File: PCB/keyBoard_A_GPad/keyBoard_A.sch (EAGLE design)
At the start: 289 parts, among them IC1 74HC04N, IC2 LMV358IDGKR, J1 J, J10 J, J11 J, J12 J, J13 J, J14 J, J15 J, J16 J, J17 J, J18 J, J19 J, J2 J, J20 J, J21 J, J22 J, J23 J, J24 J, J25 J, J26 J, J27 J, J28 J, J29 J, J3 J, J30 J, J31 J, J32 J, J33 J, J34 J, J35 J, J36 J, J37 J, J38 J, J39 J, J4 J, J40 J, J41 J, J42 J, J43 J, J44 J, J45 J, J47 USB MICRO, J5 J, J6 J, J7 J, J8 J, J9 J, Y1 16MHz KX-7, Y2 16MHz KX-7

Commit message: add kesize table. bad pcb a b
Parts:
- added 2D1: 74HC138N, detali2:74AC138N
- added 2D2: 74HC04N, detali2:74ALS04N
- added C19: 100n, rcl:C-EUC0805
- added C20: 100n, rcl:C-EUC1206
- added D49, D50, D51, D52, D53, D54, D55, D56, D57, D58, D59, D60, D61, D62, D63, D64, D64B, D65, D66, D67, D67B, D68, D69, D70, D71, D72, D73, D74, D75, D76, D77, D78, D79, D80, D81, D82, D83, D84, D85, D86, D87, D88, D89, D92, D93: LL4148, detali:LL4148
- added J46, J48, J49, J50, J51, J52, J53, J54, J55, J56, J57, J58, J59, J60, J61, J62, J63, J64, J65, J66, J67, J68, J69, J70, J71, J72, J73, J74, J75, J76, J77, J78, J79, J80, J81, J82, J83, J84, J85, J86, J87, J88, J89, J90, J91, J92, J93, J94, J95, J96: J, detali2:J
- added JA47, JA48, JA49, JA50, JA51, JA52, JA53, JA54, JA55, JA56, JA57, JA58, JA59, JA60, JA61, JA62, JA63, JA64, JA65, JA66, JA67, JA67B, JA67B1, JA68, JA69, JA70, JA71, JA72, JA73, JA74, JA74B, JA75, JA76, JA77, JA78, JA79, JA80, JA81, JA82, JA83, JA84, JA85, JA86, JA87, JB47, JB48, JB49, JB50, JB51, JB52, JB53, JB54, JB55, JB56, JB57, JB58, JB59, JB60, JB61, JB62, JB63, JB64, JB65, JB66, JB67, JB67B, JB68, JB69, JB70, JB71, JB72, JB73, JB74, JB74B, JB75, JB76, JB77, JB78, JB79, JB80, JB81, JB82, JB83, JB84, JB85, JB86, JB87: (no value), detali:SJ
- added R16: 1k, rcl:R-EU_R0805
- added R17, R18, R19, R21, R22: 10k, rcl:R-EU_R0805
- added R20: 10k, rcl:R-EU_R1206W
- added S47: F7, cherrymx:CHERRY-MX-4P
- added S48: F8, cherrymx:CHERRY-MX-4P
- added S49: F9, cherrymx:CHERRY-MX-4P
- added S50: F10, cherrymx:CHERRY-MX-4P
- added S51: F11, cherrymx:CHERRY-MX-4P
- added S52: F12, cherrymx:CHERRY-MX-4P
- added S53: 7, cherrymx:CHERRY-MX-4P
- added S54: 8, cherrymx:CHERRY-MX-4P
- added S55: 9, cherrymx:CHERRY-MX-4P
- added S56: 0, cherrymx:CHERRY-MX-4P
- added S57: -, cherrymx:CHERRY-MX-4P
- added S58: =, cherrymx:CHERRY-MX-4P
- added S59: BS, cherrymx:CHERRY-MX-4P
- added S60: Y, cherrymx:CHERRY-MX-4P
- added S61: U, cherrymx:CHERRY-MX-4P
- added S62: I, cherrymx:CHERRY-MX-4P
- added S63: O, cherrymx:CHERRY-MX-4P
- added S64: P, cherrymx:CHERRY-MX-4P
- added S65: [, cherrymx:CHERRY-MX-4P
- added S66: ], cherrymx:CHERRY-MX-4P
- added S67: |d, cherrymx:CHERRY-MX-4P
- added S67B: |u, cherrymx:CHERRY-MX
- added S67C: |, cherrymx:CHERRY-MX-4P
- added S68: H, cherrymx:CHERRY-MX-4P
- added S69: J, cherrymx:CHERRY-MX-4P
- added S70: K, cherrymx:CHERRY-MX-4P
- added S71: L, cherrymx:CHERRY-MX-4P
- added S72: :, cherrymx:CHERRY-MX-4P
- added S73: ", cherrymx:CHERRY-MX-4P
- added S74: Del, cherrymx:CHERRY-MX-4P
- added S74A: Enter, cherrymx:CHERRY-MX-4P
- added S74B: Enter, cherrymx:CHERRY-MX
- added S75: N, cherrymx:CHERRY-MX-4P
- added S76: M, cherrymx:CHERRY-MX-4P
- added S77: <, cherrymx:CHERRY-MX-4P
- added S78: >, cherrymx:CHERRY-MX-4P
- added S79: ~, cherrymx:CHERRY-MX-4P
- added S80: ?, cherrymx:CHERRY-MX-4P
- added S81: R Shift, cherrymx:CHERRY-MX-4P
- added S82: Space, cherrymx:CHERRY-MX-4P
- added S83: FN3, cherrymx:CHERRY-MX-4P
- added S84: R_Alt, cherrymx:CHERRY-MX-4P
- added S85: RCtrl, cherrymx:CHERRY-MX-4P
- added S86: PrtScr, cherrymx:CHERRY-MX-4P
- added S87: FN2, cherrymx:CHERRY-MX-4P
- added SV4: CON_KB_B, detali2:FE12-1
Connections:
- new net +3VD: 2D2P.VCC, C20.1, D92.C
- new net 2I: 2D1A.Y1, D50.C, J95.P$1
- new net 8J: D79.C, D84.C, D85.C, D89.C, J87.P$1
- new net G1: 2D2D.I, JA47.2, JA48.2, JA49.2, JA53.2, JA60.2, JA68.2, JA75.2, JA82.2, R17.2
- new net G2: J63.P$2, JA54.2, JA55.2, JA56.2, JA61.2, JA69.2, JA70.2, JA76.2, JA77.2, R18.2
- new net G3: J57.P$2, JA62.2, JA63.2, JA71.2
- new net G4: J76.P$2, JA50.2, JA51.2, JA57.2, JA64.2, JA72.2, JA78.2, JA79.2, JA87.2
- new net G5: J62.P$2, JA52.2, JA58.2, JA65.2, JA66.2, JA73.2, JA80.2, JA83.2, JA84.2
- new net G6: J59.P$2, JA59.2, JA67.2, JA67B.2, JA67B1.2, JA74B.2, JA81.2, JA85.2, JA86.2, JB74.1
- new net GG5: 2D2E.I, J61.P$1, R21.2
- new net N$107: JB52.2, S52G$1.PIN-1
- new net N$151: JB63.2, S63G$1.PIN-1
- new net N$229: JB74.2, S74AG$1.PIN-1, S74B.PIN-1
- new net N$230: JA74.1, S74AG$1.PIN-2, S74B.PIN-2
- new net N$233: JB47.2, S47G$1.PIN-1
- new net N$234: JB53.2, S53G$1.PIN-1
- new net N$235: JB60.2, S60G$1.PIN-1
- new net N$236: JB68.2, S68G$1.PIN-1
- new net N$237: JB75.2, S75G$1.PIN-1
- new net N$238: JB82.2, S82G$1.PIN-1
- new net N$239: JB48.2, S48G$1.PIN-1
- new net N$240: JB54.2, S54G$1.PIN-1
- new net N$241: JB61.2, S61G$1.PIN-1
- new net N$242: JB69.2, S69G$1.PIN-1
- new net N$243: JB49.2, S49G$1.PIN-1
- new net N$244: JB55.2, S55G$1.PIN-1
- new net N$245: JB70.2, S70G$1.PIN-1
- new net N$246: JB77.2, S77G$1.PIN-1
- new net N$247: JB56.2, S56G$1.PIN-1
- new net N$248: JB51.2, S51G$1.PIN-1
- new net N$249: D49.A, JB47.1
- new net N$250: D55.A, JB53.1
- new net N$251: D62.A, JB60.1
- new net N$252: D70.A, JB68.1
- new net N$253: D77.A, JB75.1
- new net N$254: D84.A, JB82.1
- new net N$255: D50.A, JB48.1
- new net N$256: D56.A, JB54.1
- new net N$257: D63.A, JB61.1
- new net N$258: D71.A, JB69.1
- new net N$259: D78.A, JB76.1
- new net N$260: D85.A, JB83.1
- new net N$261: D51.A, JB49.1
- new net N$262: D57.A, JB55.1
- new net N$263: D64.A, JB62.1
- new net N$264: D72.A, JB70.1
- new net N$265: D79.A, JB77.1
- new net N$266: D86.A, JB84.1
- new net N$267: D52.A, JB50.1
- new net N$268: D58.A, JB56.1
- new net N$269: D65.A, JB63.1
- new net N$270: D73.A, JB71.1
- new net N$271: D80.A, JB78.1
- new net N$272: D87.A, JB85.1
- new net N$274: D53.A, JB51.1
- new net N$275: D59.A, JB57.1
- new net N$277: D66.A, JB64.1
- new net N$278: D74.A, JB72.1
- new net N$279: D81.A, JB79.1
- new net N$280: D88.A, JB86.1
- new net N$281: D54.A, JB52.1
- new net N$282: D60.A, JB58.1
- new net N$283: D67.A, JB65.1
- new net N$285: D75.A, JB73.1
- new net N$286: D82.A, JB80.1
- new net N$287: D61.A, JB59.1
- new net N$288: D68.A, JB66.1
- new net N$289: D69.A, JB67.1
- new net N$290: D83.A, JB81.1
- new net N$291: JA47.1, S47G$1.PIN-2
- new net N$292: JA53.1, S53G$1.PIN-2
- new net N$293: JA60.1, S60G$1.PIN-2
- new net N$294: JA68.1, S68G$1.PIN-2
- new net N$295: JA75.1, S75G$1.PIN-2
- new net N$296: JA82.1, S82G$1.PIN-2
- new net N$297: JA48.1, S48G$1.PIN-2
- new net N$298: JA54.1, S54G$1.PIN-2
- new net N$299: JA61.1, S61G$1.PIN-2
- new net N$300: JA69.1, S69G$1.PIN-2
- new net N$301: JA49.1, S49G$1.PIN-2
- new net N$302: JA55.1, S55G$1.PIN-2
- new net N$303: JA70.1, S70G$1.PIN-2
- new net N$304: JA77.1, S77G$1.PIN-2
- new net N$305: JA56.1, S56G$1.PIN-2
- new net N$306: JA63.1, S63G$1.PIN-2
- new net N$307: JA51.1, S51G$1.PIN-2
- new net N$308: JA52.1, S52G$1.PIN-2
- new net N$309: D64B.A, JB74B.1
- new net N$310: JA67B1.1, S67B.PIN-2
- new net N$311: JA67B.1, S67CG$1.PIN-1
- new net N$312: D76.A, JA74.2
- new net N$313: JB67.2, S67G$1.PIN-2
- new net N$314: JA67.1, S67G$1.PIN-1
- new net N$315: JB81.2, S81G$1.PIN-2
- new net N$316: JA81.1, S81G$1.PIN-1
- new net N$317: JB59.2, S59G$1.PIN-2
- new net N$318: JA59.1, S59G$1.PIN-1
- new net N$319: JB85.2, S85G$1.PIN-2
- new net N$320: JA85.1, S85G$1.PIN-1
- new net N$321: JB74B.2, S74G$1.PIN-2
- new net N$322: JA74B.1, S74G$1.PIN-1
- new net N$323: J96.P$1, S67B.PIN-1, S67CG$1.PIN-2
- new net N$324: JA87.1, S87G$1.PIN-1
- new net N$325: JB87.2, S87G$1.PIN-2
- new net N$326: D89.A, JB87.1
- new net N$327: JB50.2, S50G$1.PIN-2
- new net N$328: JA50.1, S50G$1.PIN-1
- new net N$329: JB78.2, S78G$1.PIN-2
- new net N$330: JA78.1, S78G$1.PIN-1
- new net N$331: D67B.A, JB67B.1
- new net N$332: JB58.2, S58G$1.PIN-2
- new net N$333: JB65.2, S65G$1.PIN-2
- new net N$334: JA65.1, S65G$1.PIN-1
- new net N$335: JA58.1, S58G$1.PIN-1
- new net N$336: JB66.2, S66G$1.PIN-1
- new net N$337: JA66.1, S66G$1.PIN-2
- new net N$338: JB79.2, S79G$1.PIN-2
- new net N$339: JA79.1, S79G$1.PIN-1
- new net N$340: JB83.2, S83G$1.PIN-2
- new net N$341: JA83.1, S83G$1.PIN-1
- new net N$342: JB73.2, S73G$1.PIN-2
- new net N$343: JA73.1, S73G$1.PIN-1
- new net N$344: JA80.1, S80G$1.PIN-1
- new net N$345: JB80.2, S80G$1.PIN-2
- new net N$346: JB84.2, S84G$1.PIN-2
- new net N$347: JA84.1, S84G$1.PIN-1
- new net N$349: JB57.2, S57G$1.PIN-2
- new net N$350: JA57.1, S57G$1.PIN-1
- new net N$351: JA64.1, S64G$1.PIN-1
- new net N$352: JB64.2, S64G$1.PIN-2
- new net N$353: JB72.2, S72G$1.PIN-2
- new net N$354: JA72.1, S72G$1.PIN-1
- new net N$355: J48.P$1, J49.P$2
- new net N$356: JB62.2, S62G$1.PIN-2
- new net N$357: JA62.1, S62G$1.PIN-1
- new net N$358: JB71.2, S71G$1.PIN-1
- new net N$359: JA71.1, S71G$1.PIN-2
- new net N$360: 2D1A.G1, R16.2
- new net N$361: JB76.2, S76G$1.PIN-2
- new net N$362: JA76.1, S76G$1.PIN-1
- new net N$363: 2D2C.O, SV4.7
- new net N$364: 2D2B.O, SV4.6
- new net N$365: 2D2A.O, SV4.5
- new net N$366: 2D2F.O, J64.P$2
- new net N$367: 2D2D.O, J69.P$2
- new net N$368: J57.P$1, J58.P$2
- new net N$369: J59.P$1, J60.P$2
- new net N$370: 2D2A.I, J63.P$1
- new net N$371: J64.P$1, SV4.4
- new net N$372: J65.P$1, SV4.3
- new net N$373: J65.P$2, J66.P$1
- new net N$374: 2D2E.O, J66.P$2
- new net N$375: J67.P$1, SV4.2
- new net N$376: J67.P$2, J68.P$1
- new net N$377: J68.P$2, J69.P$1
- new net N$378: D92.A, D93.C
- new net N$379: J70.P$1, J73.P$2
- new net N$380: J71.P$1, J74.P$2
- new net N$381: J72.P$1, J75.P$2
- new net N$382: J73.P$1, J77.P$2
- new net N$383: J74.P$1, J78.P$2
- new net N$384: J75.P$1, J79.P$2
- new net N$385: J79.P$1, J80.P$2
- new net N$386: J77.P$1, J81.P$2
- new net N$387: J78.P$1, J82.P$2
- new net N$388: J80.P$1, J83.P$2
- new net N$389: J82.P$1, J84.P$2
- new net N$391: J81.P$1, J85.P$2
- new net N$392: 2D1A.A, J83.P$1
- new net N$393: 2D1A.B, J84.P$1
- new net N$394: 2D1A.C, J85.P$1
- new net N$395: 2D1A.Y0, J86.P$2
- new net N$396: JB86.2, S86G$1.PIN-1
- new net N$397: JA86.1, S86G$1.PIN-2
- new net N$398: 2D1A.Y7, J88.P$2
- new net N$399: J90.P$1, J91.P$2
- new net N$400: 2D1A.Y4, J90.P$2
- new net N$401: J89.P$2, J92.P$1
- new net N$402: J93.P$1, J94.P$2
- new net N$403: 2D1A.Y6, J93.P$2
- new net N$404: 2D1A.Y5, J92.P$2
- new net N$405: J46.P$1, J95.P$2
- new net N$406: J96.P$2, JB67B.2
- new net PG3: 2D2B.I, J58.P$1, R19.2
- new net PG4: 2D2C.I, J76.P$1, R20.2
- new net PG5: J61.P$2, J62.P$1
- new net PG6: 2D2F.I, J60.P$1, R22.2
- net +5V: now also 2D1P.VCC, C19.1, D93.A, R16.1, R17.1, R18.1, R19.1, R20.1, R21.1, R22.1, SV4.11
- net 1: now also D51.C, D52.C, D54.C, D58.C, D64B.C, J86.P$1
- net 2: now also D53.C, D60.C, D61.C, J46.P$2, J53.P$2
- net 2J: now also D57.C, J53.P$1
- net 3: now also D49.C, D56.C, D59.C, D65.C, J48.P$2
- net 3J: now also D67B.C, D68.C, J49.P$1, J88.P$1
- net 4: now also D67.C, D76.C, J50.P$1, J91.P$1
- net 4J: now also D66.C, D73.C, J50.P$2, J54.P$2
- net 4J2: now also D55.C, D63.C, J54.P$1
- net 5: now also D69.C, D75.C, J51.P$1, J89.P$1
- net 5J: now also D62.C, D64.C, D71.C, D74.C, J51.P$2
- net 6: now also D81.C, D82.C, D83.C, J55.P$2, J94.P$1
- net 6J2: now also D72.C, J55.P$1, J56.P$2
- net 6J3: now also D70.C, J56.P$1
- net 7: now also 2D1A.Y2, D86.C, D87.C, J52.P$1
- net 7J: now also D77.C, D78.C, D80.C, J52.P$2
- net 8: now also 2D1A.Y3, D88.C, J87.P$2
- net D1: now also J70.P$2, SV4.10
- net D2: now also J71.P$2, SV4.9
- net D3: now also J72.P$2, SV4.8
- net GND: now also 2D1A.G2A, 2D1A.G2B, 2D1P.GND, 2D2P.GND, C19.2, C20.2, SV4.1

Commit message: new pcb >
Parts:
- removed 1D0: ATMEGA32U4, detali_main:SMARTPRJ_ATMEGA32U4-XUAU
- removed C1, C2: 22p, SmartPrj:C-EUC0603
- removed R1: 1M, SmartPrj:R-EU_R0603
- removed R2, R7: (no value), rcl:R-EU_M0805
- removed S74B: Enter, cherrymx:CHERRY-MX
- removed SV1: (no value), detali_main:FE12-1
- removed SV2: CON_KB_N, detali_main:FE09-1
- removed U$52: FE1.1S, imcom:FE1.1S
- removed Y2: 16MHz KX-7, SmartPrj:CRYSTAL-3.2-2.5
- added 1D2: ATMEGA32U4, detali_main:SMARTPRJ_ATMEGA32U4-XUAU
- added C21, C23: 22p, SmartPrj:C-EUC0603
- added R23, R25: (no value), rcl:R-EU_M0805
- added R24: 1M, SmartPrj:R-EU_R0603
- added S44A: Fn1, cherrymx:CHERRY-MX
- added SV5: CON_KB_N, detali_main:FE09-1
- added SV6: (no value), detali_main:FE12-1
- added U$102: FE1.1S, imcom:FE1.1S
- added U$81: CHERRY-MX, cherrymx:CHERRY-MX
- added Y3: 16MHz KX-7, SmartPrj:CRYSTAL-3.2-2.5
- S44: value F1 -> FN1
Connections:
- removed net N$117: JA44.1, S44G$1.PIN-2
- removed net N$197: 1D0.(#HWB)PE2, R2.1
- removed net N$284: 1D0.(PCINT7/OC0A/OC1C/#RTS)PB7, R7.1
- removed net N$65: JB44.2, S44G$1.PIN-1
- removed net XTAL3: 1D0.XTAL2, C1.2, R1.2, Y2.C2
- removed net XTAL4: 1D0.XTAL1, C2.1, R1.1, Y2.C1
- new net +5V_B: 2D1P.VCC, C19.1, D93.A, R16.1, R17.1, R18.1, R19.1, R20.1, R21.1, R22.1, SV4.11
- new net AFN1A: JB44.2, S44A.PIN-1, S44G$1.PIN-1
- new net AFN1B: JA44.1, S44A.PIN-2, S44G$1.PIN-2
- new net B1: D51.C, D52.C, D54.C, D58.C, D64B.C, J86.P$1
- new net B2: D53.C, D60.C, D61.C, J46.P$2, J53.P$2
- new net B2J: D57.C, J53.P$1
- new net B3: D49.C, D56.C, D59.C, D65.C, J48.P$2
- new net B3J: D67B.C, D68.C, J49.P$1, J88.P$1
- new net B4: D67.C, D76.C, J50.P$1, J91.P$1
- new net B4J: D66.C, D73.C, J50.P$2, J54.P$2
- new net B4J2: D55.C, D63.C, J54.P$1
- new net B5: D69.C, D75.C, J51.P$1, J89.P$1
- new net B5J: D62.C, D64.C, D71.C, D74.C, J51.P$2
- new net B6: D81.C, D82.C, D83.C, J55.P$2, J94.P$1
- new net B6J2: D72.C, J55.P$1, J56.P$2
- new net B6J3: D70.C, J56.P$1
- new net B7: 2D1A.Y2, D86.C, D87.C, J52.P$1
- new net B7J: D77.C, D78.C, D80.C, J52.P$2
- new net B8: 2D1A.Y3, D88.C, J87.P$2
- new net BD1: J70.P$2, SV4.10
- new net BD2: J71.P$2, SV4.9
- new net BD3: J72.P$2, SV4.8
- new net CD1: SV5.8, SV6.10
- new net CD2: SV5.7, SV6.9
- new net CD3: SV5.6, SV6.8
- new net GND_B: 2D1A.G2A, 2D1A.G2B, 2D1P.GND, 2D2P.GND, C19.2, C20.2, SV4.1
- new net N$506: 1D2.(PCINT7/OC0A/OC1C/#RTS)PB7, R23.1
- new net N$507: 1D2.(#HWB)PE2, R25.1
- new net XTAL5: 1D2.XTAL2, C21.2, R24.2, Y3.C2
- new net XTAL6: 1D2.XTAL1, C23.1, R24.1, Y3.C1
- net +5V: now also R25.2, SV5.9, SV6.11; no longer 2D1P.VCC, C19.1, D93.A, R16.1, R17.1, R18.1, R19.1, R2.2, R20.1, R21.1, R22.1, SV1.11, SV2.9, SV4.11
- net 1: no longer D51.C, D52.C, D54.C, D58.C, D64B.C, J86.P$1
- net 2: no longer D53.C, D60.C, D61.C, J46.P$2, J53.P$2
- net 2J: no longer D57.C, J53.P$1
- net 3: no longer D49.C, D56.C, D59.C, D65.C, J48.P$2
- net 3J: no longer D67B.C, D68.C, J49.P$1, J88.P$1
- net 4: no longer D67.C, D76.C, J50.P$1, J91.P$1
- net 4J: no longer D66.C, D73.C, J50.P$2, J54.P$2
- net 4J2: no longer D55.C, D63.C, J54.P$1
- net 5: no longer D69.C, D75.C, J51.P$1, J89.P$1
- net 5J: no longer D62.C, D64.C, D71.C, D74.C, J51.P$2
- net 6: no longer D81.C, D82.C, D83.C, J55.P$2, J94.P$1
- net 6J2: no longer D72.C, J55.P$1, J56.P$2
- net 6J3: no longer D70.C, J56.P$1
- net 7: no longer 2D1A.Y2, D86.C, D87.C, J52.P$1
- net 7J: no longer D77.C, D78.C, D80.C, J52.P$2
- net 8: no longer 2D1A.Y3, D88.C, J87.P$2
- net D1: no longer J70.P$2, SV1.10, SV2.8, SV4.10
- net D2: no longer J71.P$2, SV1.9, SV2.7, SV4.9
- net D3: no longer J72.P$2, SV1.8, SV2.6, SV4.8
- net GND: now also C21.1, C23.2, SV5.1, SV6.1, Y3.GND@1, Y3.GND@2; no longer 2D1A.G2A, 2D1A.G2B, 2D1P.GND, 2D2P.GND, C1.1, C19.2, C2.2, C20.2, SV1.1, SV2.1, SV4.1, Y2.GND@1, Y2.GND@2
- net KBB1: now also SV6.2; no longer SV1.2
- net KBB2: now also SV6.3; no longer SV1.3
- net KBB3: now also SV6.4; no longer SV1.4
- net KBB4: now also SV6.5; no longer SV1.5
- net KBB5: now also SV6.6; no longer SV1.6
- net KBB6: now also SV6.7; no longer SV1.7
- net KBN1: now also SV5.2; no longer SV2.2
- net KBN2: now also SV5.3; no longer SV2.3
- net KBN3: now also SV5.5; no longer SV2.5
- net LED_NUM: now also SV5.4; no longer SV2.4
- net N$229: no longer S74B.PIN-1
- net N$230: no longer S74B.PIN-2
- net N$238: now also U$81.PIN-2
- net N$296: now also U$81.PIN-1
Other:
- note added: "LEFT KB"

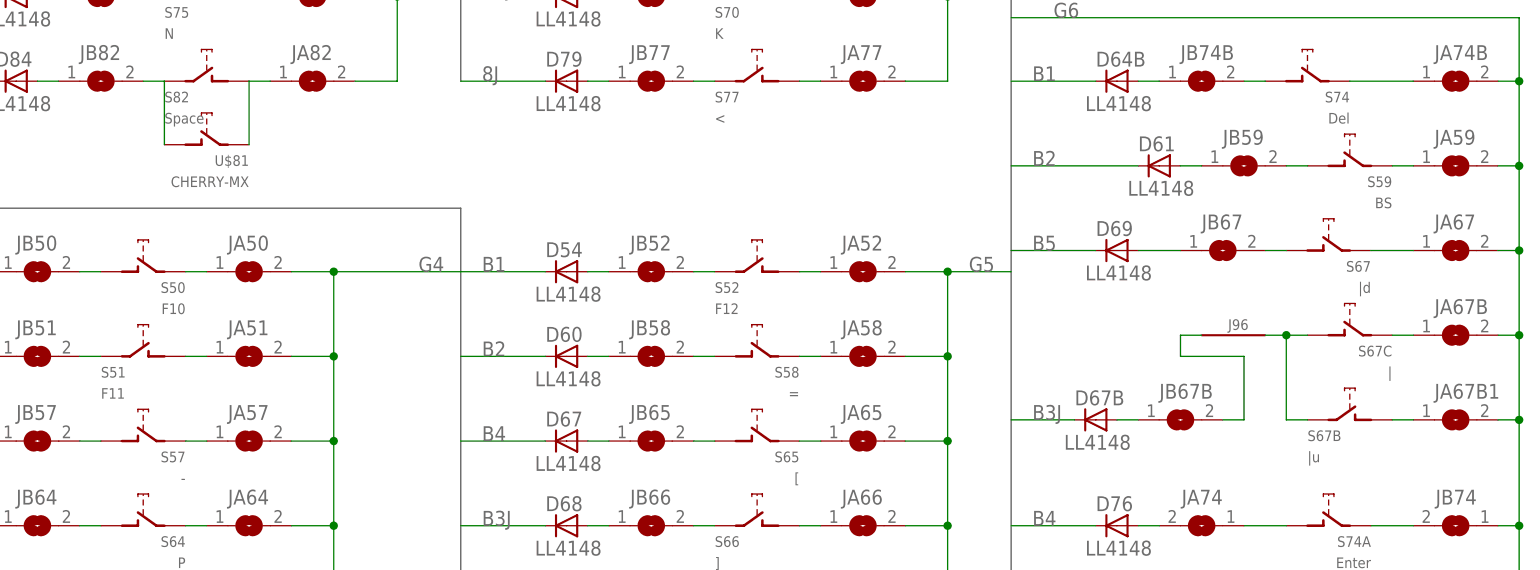
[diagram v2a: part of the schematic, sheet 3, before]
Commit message: pcb b > ab
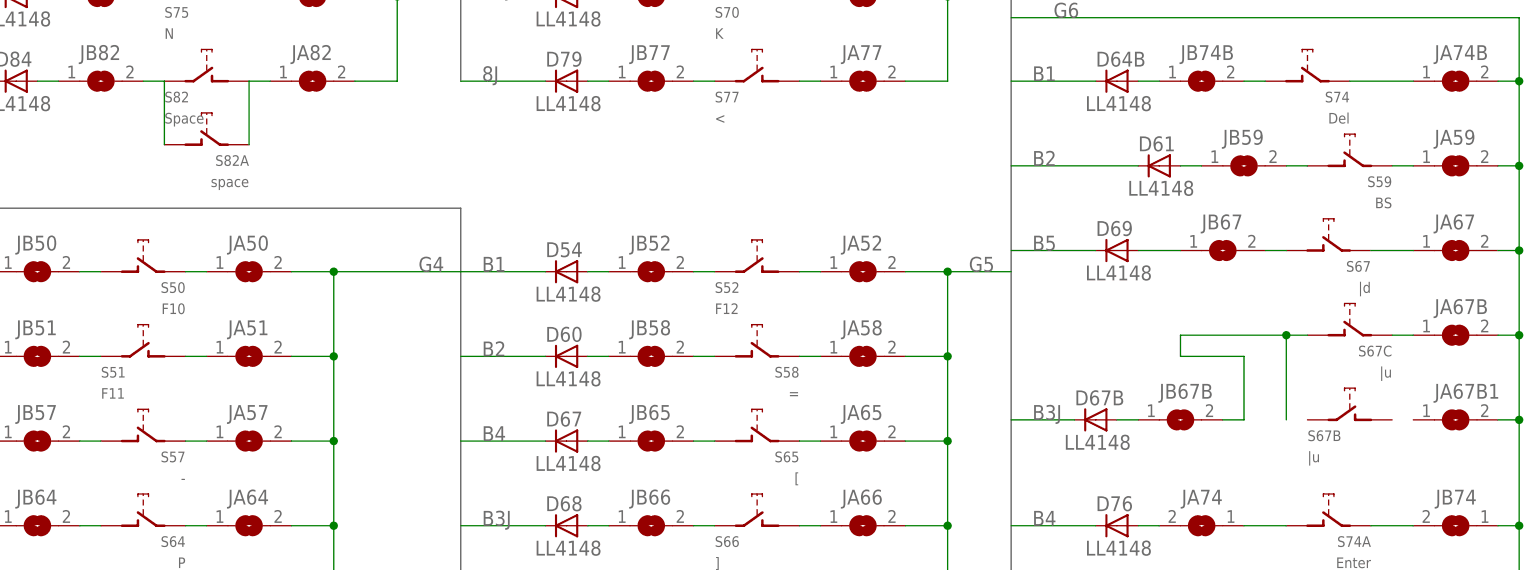
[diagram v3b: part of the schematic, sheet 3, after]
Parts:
- removed J96: J, detali2:J
- S67C: value | -> |u
- S82A: value CHERRY-MX -> space
- renumbered U$81 to S82A
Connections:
- removed net N$310: JA67B1.1, S67B.PIN-2
- removed net N$323: J96.P$1, S67B.PIN-1, S67CG$1.PIN-2
- net N$406: now also S67CG$1.PIN-2; no longer J96.P$2
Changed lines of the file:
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@@
 <part name="JA74B" library="detali" deviceset="SJ" device=""/>
 <part name="D64B" library="detali" deviceset="LL4148" device=""/>
-<part name="S67C" library="cherrymx" deviceset="CHERRY-MX-4P" device="" value="|"/>
+<part name="S67C" library="cherrymx" deviceset="CHERRY-MX-4P" device="" value="|u"/>
 <part name="2D1" library="detali2" deviceset="74*138" device="N" technology="AC" value="74HC138N"/>
 <part name="JA67B" library="detali" deviceset="SJ" device=""/>
@@
 <part name="R21" library="rcl" deviceset="R-EU_" device="R0805" value="10k"/>
 <part name="R22" library="rcl" deviceset="R-EU_" device="R0805" value="10k"/>
-<part name="J96" library="detali2" deviceset="J" device="" value=""/>
 <part name="1D2" library="detali_main" deviceset="SMARTPRJ_ATMEGA32U4-XU" device="AU" value="ATMEGA32U4"/>
 <part name="SV5" library="detali_main" deviceset="FE09-1" device="" value="CON_KB_N"/>
@@
 <part name="P+19" library="supply1" deviceset="+5V" device=""/>
 <part name="S44A" library="cherrymx" deviceset="CHERRY-MX" device="" value="Fn1"/>
-<part name="U$81" library="cherrymx" deviceset="CHERRY-MX" device=""/>
+<part name="S82A" library="cherrymx" deviceset="CHERRY-MX" device="" value="space"/>
 </parts>
 <sheets>
@@
 <attribute name="VALUE" x="110.49" y="224.282" size="1.778" layer="96" rot="R180"/>
 </instance>
-<instance part="J96" gate="G$1" x="175.26" y="73.66" smashed="yes">
-<attribute name="NAME" x="175.895" y="74.295" size="1.27" layer="95"/>
-</instance>
-<instance part="U$81" gate="G$1" x="53.34" y="96.52" rot="MR0"/>
+<instance part="S82A" gate="G$1" x="53.34" y="96.52" rot="MR0"/>
 </instances>
 <busses>
@@
 <pinref part="JB82" gate="1" pin="2"/>
 <wire x1="45.72" y1="104.14" x2="48.26" y2="104.14" width="0.1524" layer="91"/>
-<pinref part="U$81" gate="G$1" pin="PIN-2"/>
+<pinref part="S82A" gate="G$1" pin="PIN-2"/>
 <wire x1="48.26" y1="96.52" x2="48.26" y2="104.14" width="0.1524" layer="91"/>
 </segment>
@@
 <pinref part="JA82" gate="1" pin="1"/>
 <wire x1="60.96" y1="104.14" x2="58.42" y2="104.14" width="0.1524" layer="91"/>
-<pinref part="U$81" gate="G$1" pin="PIN-1"/>
+<pinref part="S82A" gate="G$1" pin="PIN-1"/>
 <wire x1="58.42" y1="96.52" x2="58.42" y2="104.14" width="0.1524" layer="91"/>
 </segment>
@@
 </segment>
 </net>
-<net name="N$310" class="0">
-<segment>
-<pinref part="S67B" gate="G$1" pin="PIN-2"/>
-<wire x1="195.58" y1="63.5" x2="198.12" y2="63.5" width="0.1524" layer="91"/>
-<pinref part="JA67B1" gate="1" pin="1"/>
-</segment>
-</net>
 <net name="N$311" class="0">
 <segment>
@@
 </segment>
 </net>
-<net name="N$323" class="0">
-<segment>
-<pinref part="S67B" gate="G$1" pin="PIN-1"/>
-<pinref part="S67C" gate="G$1" pin="PIN-2"/>
-<wire x1="182.88" y1="63.5" x2="185.42" y2="63.5" width="0.1524" layer="91"/>
-<wire x1="182.88" y1="73.66" x2="185.42" y2="73.66" width="0.1524" layer="91"/>
-<wire x1="182.88" y1="63.5" x2="182.88" y2="73.66" width="0.1524" layer="91"/>
-<pinref part="J96" gate="G$1" pin="P$1"/>
-<wire x1="180.34" y1="73.66" x2="182.88" y2="73.66" width="0.1524" layer="91"/>
-<junction x="182.88" y="73.66"/>
-</segment>
-</net>
 <net name="N$324" class="0">
 <segment>
@@
 <wire x1="177.8" y1="71.12" x2="170.18" y2="71.12" width="0.1524" layer="91"/>
 <wire x1="170.18" y1="71.12" x2="170.18" y2="73.66" width="0.1524" layer="91"/>
-<pinref part="J96" gate="G$1" pin="P$2"/>
-<wire x1="170.18" y1="73.66" x2="172.72" y2="73.66" width="0.1524" layer="91"/>
+<pinref part="S67C" gate="G$1" pin="PIN-2"/>
+<wire x1="182.88" y1="73.66" x2="185.42" y2="73.66" width="0.1524" layer="91"/>
+<wire x1="182.88" y1="63.5" x2="182.88" y2="73.66" width="0.1524" layer="91"/>
+<junction x="182.88" y="73.66"/>
+<wire x1="170.18" y1="73.66" x2="182.88" y2="73.66" width="0.1524" layer="91"/>
 </segment>
 </net>
